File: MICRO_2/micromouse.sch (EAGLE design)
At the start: 26 parts

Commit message: Add files via upload
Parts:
- removed C1: (no value), capacitor-wima:C2,5-3
- removed R1, R2, R3, R4, R5: 10k, rcl:R-US_0204/5
- removed R10, R6, R7, R8, R9: 330, rcl:R-US_0204/5
- removed U$15: VOLTAGE_REGULATOR, VOLTAGE_REGULATOR:VOLTAGE_REGULATOR
- U$1: value TEENSY3.2 -> MOTOR_ENCODER; device teensy_3.2:TEENSY3.2 -> MOTOR_ENCODER:MOTOR_ENCODER
- U$10, U$11, U$12: value IR_EMITTER -> IR_RECIEVER; device IR_EMITTER:IR_EMITTER -> IR_RECIEVER:IR_RECIEVER
- U$13, U$14: value MOTOR_ENCODER -> IR_RECIEVER; device MOTOR_ENCODER:MOTOR_ENCODER -> IR_RECIEVER:IR_RECIEVER
- U$2: value MOTOR_DRIVER -> MOTOR_ENCODER; device motor_driver:MOTOR_DRIVER -> MOTOR_ENCODER:MOTOR_ENCODER
- U$3: value IR_RECIEVER -> TEENSY_3.1-3.2_DIL; device IR_RECIEVER:IR_RECIEVER -> Teensy_3_and_LC_Series_Boards_v1.4:TEENSY_3.1-3.2_DIL
- U$4: value IR_RECIEVER -> MOTOR_DRIVER; device IR_RECIEVER:IR_RECIEVER -> motor_driver:MOTOR_DRIVER
- U$5, U$6, U$7: value IR_RECIEVER -> IR_EMITTER; device IR_RECIEVER:IR_RECIEVER -> IR_EMITTER:IR_EMITTER
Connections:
- removed net GND: C1.2, R1.1, R2.2, R3.1, R4.1, R5.2, U$1.GND, U$10.EMI_CATHODE, U$11.EMI_CATHODE, U$12.EMI_CATHODE, U$13.GND, U$14.GND, U$15.GND, U$2.L_GND_1, U$2.L_GND_2, U$2.R_GND_1, U$2.R_GND_2, U$8.EMI_CATHODE, U$9.EMI_CATHODE
- removed net N$1: U$1.2, U$2.M1_ENABLE
- removed net N$10: R6.1, U$1.0
- removed net N$11: R7.1, U$9.EMI_ANODE
- removed net N$12: R7.2, U$1.7
- removed net N$13: R8.1, U$10.EMI_ANODE
- removed net N$14: R8.2, U$1.8
- removed net N$15: R9.1, U$11.EMI_ANODE
- removed net N$16: R9.2, U$1.11
- removed net N$17: R10.1, U$12.EMI_ANODE
- removed net N$18: R10.2, U$1.12
- removed net N$19: R1.2, U$1.15, U$4.REC_CATHODE
- removed net N$2: U$1.3, U$2.M1_FWD_PWN
- removed net N$20: R2.1, U$1.16, U$5.REC_CATHODE
- removed net N$21: R4.2, U$1.17, U$6.REC_CATHODE
- removed net N$22: R5.1, U$1.18, U$7.REC_CATHODE
- removed net N$24: R3.2, U$1.14, U$3.REC_CATHODE
- removed net N$25: U$13.M1, U$2.L_M1_1
- removed net N$26: U$1.20, U$14.OUTB
- removed net N$27: U$1.13, U$13.OUTA
- removed net N$28: U$1.21, U$14.OUTA
- removed net N$29: U$1.19, U$13.OUTB
- removed net N$3: U$13.M2, U$2.L_M1_2
- removed net N$30: C1.1, U$1.26, U$13.VCC, U$14.VCC, U$15.VOUT, U$2.L_5V, U$2.R_5V
- removed net N$32: U$14.M1, U$2.R_M2_1
- removed net N$36: U$1.24, U$3.REC_ANODE, U$4.REC_ANODE, U$5.REC_ANODE, U$6.REC_ANODE, U$7.REC_ANODE
- removed net N$4: U$1.1, U$2.M2_ENABLE
- removed net N$5: U$1.5, U$2.M2_REV_PWM
- removed net N$6: U$14.M2, U$2.R_M2_2
- removed net N$7: U$1.6, U$2.M2_FWD_PWM
- removed net N$8: U$1.4, U$2.M1_REV_PWN
- removed net N$9: R6.2, U$8.EMI_ANODE

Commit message: Add files via upload
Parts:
- removed U$13, U$14: IR_RECIEVER, IR_RECIEVER:IR_RECIEVER
- added R1, R3, R5: 330, rcl:R-US_0207/10
- added R2, R4: 10K, rcl:R-US_0207/10
- added R6: 10k, rcl:R-US_0207/10
- U$10: value IR_RECIEVER -> VOLTAGE_REGULATOR; device IR_RECIEVER:IR_RECIEVER -> VOLTAGE_REGULATOR:VOLTAGE_REGULATOR
- U$11: value IR_RECIEVER -> BATTERY_INPUT; device IR_RECIEVER:IR_RECIEVER -> Battery_input:BATTERY_INPUT
- U$5, U$8: value IR_EMITTER -> IR_RECIEVER; device IR_EMITTER:IR_EMITTER -> IR_RECIEVER:IR_RECIEVER
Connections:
- new net N$1: U$10.VIN, U$11.VIN
- new net N$10: U$3.13/SCK/LED, U$4.M2_ENABLE
- new net N$11: U$1.M1, U$4.L_M1_1
- new net N$12: U$1.M2, U$4.L_M1_2
- new net N$13: U$2.M1, U$4.R_M2_1
- new net N$14: U$2.M2, U$4.R_M2_2
- new net N$15: U$1.OUTA, U$3.10/TX2/PWM
- new net N$16: U$1.OUTB, U$3.11/MOSI
- new net N$17: U$2.OUTB, U$3.8/TX3
- new net N$18: U$2.OUTA, U$3.9/RX2/PWM
- new net N$2: U$1.GND, U$10.GND, U$11.GND, U$2.GND, U$3.GND, U$4.L_GND_1, U$4.L_GND_2, U$4.R_GND_1, U$4.R_GND_2
- new net N$3: U$1.VCC, U$10.VOUT, U$2.VCC, U$3.VIN, U$4.L_5V, U$4.R_5V
- new net N$4: U$3.12/MISO, U$4.M1_ENABLE
- new net N$5: U$3.3.3V
- new net N$6: U$3.20/A6/PWM, U$4.M1_FWD_PWN
- new net N$7: U$3.21/A7/PWM, U$4.M1_REV_PWN
- new net N$8: U$3.22/A8/T/PWM, U$4.M2_REV_PWM
- new net N$9: U$3.23/A9/T/PWM, U$4.M2_FWD_PWM
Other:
- moved on the sheet: U$3

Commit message: Add files via upload
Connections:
- new net N$19: R1.2, U$3.0/RX1/T
- new net N$20: R1.1, U$9.EMI_ANODE
- new net N$21: R6.1, U$3.14/A1, U$8.REC_CATHODE
- new net N$22: R3.2, U$3.1/TX1/T
- new net N$23: R3.1, U$6.EMI_ANODE
- new net N$24: R4.1, U$12.REC_CATHODE, U$3.15/A1/T
- new net N$25: R5.2, U$3.2
- new net N$26: R5.1, U$7.EMI_ANODE
- new net N$28: R2.1, U$3.16/A2/T, U$5.REC_CATHODE
- net N$2: now also R2.2, R4.2, R6.2, U$6.EMI_CATHODE, U$7.EMI_CATHODE, U$9.EMI_CATHODE
- net N$5: now also U$12.REC_ANODE, U$5.REC_ANODE, U$8.REC_ANODE
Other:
- moved on the sheet: R1, R2, R3, R4, R5, R6

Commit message: Add files via upload
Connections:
- removed net N$2: R2.2, R4.2, R6.2, U$1.GND, U$10.GND, U$11.GND, U$2.GND, U$3.GND, U$4.L_GND_1, U$4.L_GND_2, U$4.R_GND_1, U$4.R_GND_2, U$6.EMI_CATHODE, U$7.EMI_CATHODE, U$9.EMI_CATHODE
- new net GND: R2.2, R4.2, R6.2, U$1.GND, U$10.GND, U$11.BAT_GND, U$2.GND, U$3.GND, U$4.L_GND_1, U$4.L_GND_2, U$4.R_GND_1, U$4.R_GND_2, U$6.EMI_CATHODE, U$7.EMI_CATHODE, U$9.EMI_CATHODE
- net N$1: now also U$11.BAT_7.4V; no longer U$11.VIN
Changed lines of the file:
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@@
 <net name="N$1" class="0">
 <segment>
-<pinref part="U$11" gate="G$1" pin="VIN"/>
 <wire x1="88.9" y1="-10.16" x2="88.9" y2="-22.86" width="0.1524" layer="91"/>
 <pinref part="U$10" gate="G$1" pin="VIN"/>
 <wire x1="88.9" y1="-22.86" x2="55.88" y2="-22.86" width="0.1524" layer="91"/>
 <wire x1="55.88" y1="-22.86" x2="55.88" y2="-10.16" width="0.1524" layer="91"/>
-</segment>
-</net>
-<net name="N$2" class="0">
-<segment>
-<pinref part="U$11" gate="G$1" pin="GND"/>
+<pinref part="U$11" gate="G$1" pin="BAT_7.4V"/>
+</segment>
+</net>
+<net name="GND" class="0">
+<segment>
 <wire x1="93.98" y1="-10.16" x2="93.98" y2="-15.24" width="0.1524" layer="91"/>
 <wire x1="93.98" y1="-15.24" x2="58.42" y2="-15.24" width="0.1524" layer="91"/>
@@
 <wire x1="45.72" y1="55.88" x2="45.72" y2="33.02" width="0.1524" layer="91"/>
 <junction x="45.72" y="33.02"/>
+<pinref part="U$11" gate="G$1" pin="BAT_GND"/>
 </segment>
 </net>
@@
 </sheet>
 </sheets>
+<errors>
+</errors>
 </schematic>
 </drawing>

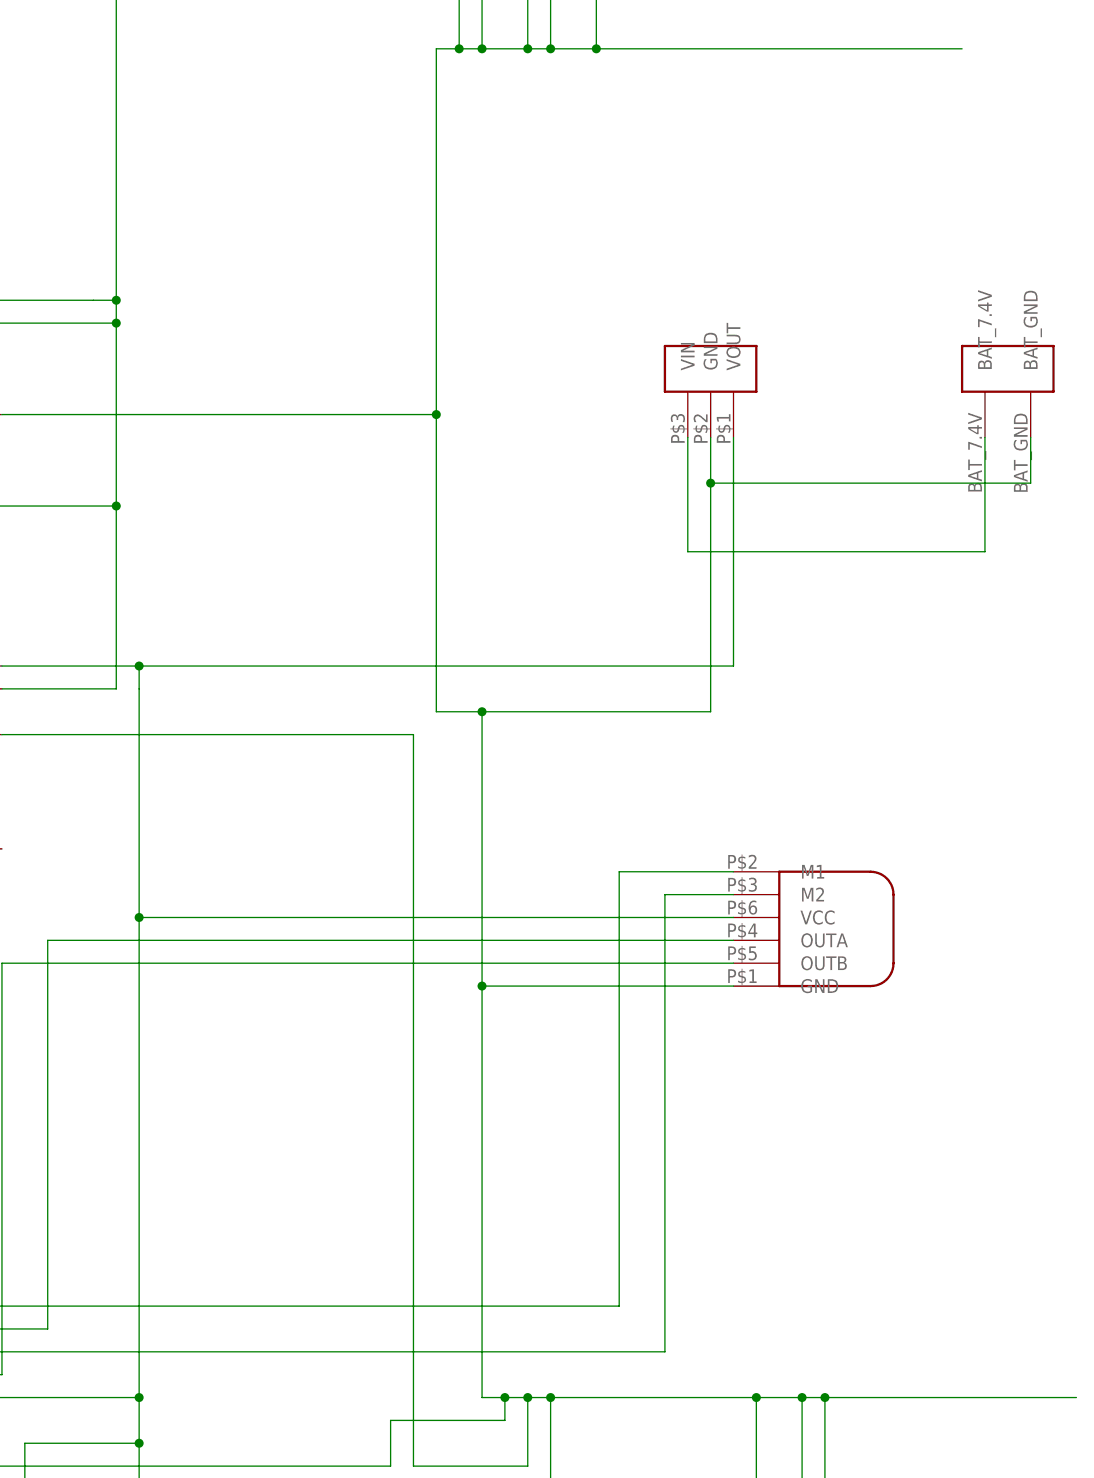
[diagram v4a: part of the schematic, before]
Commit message: added imu component
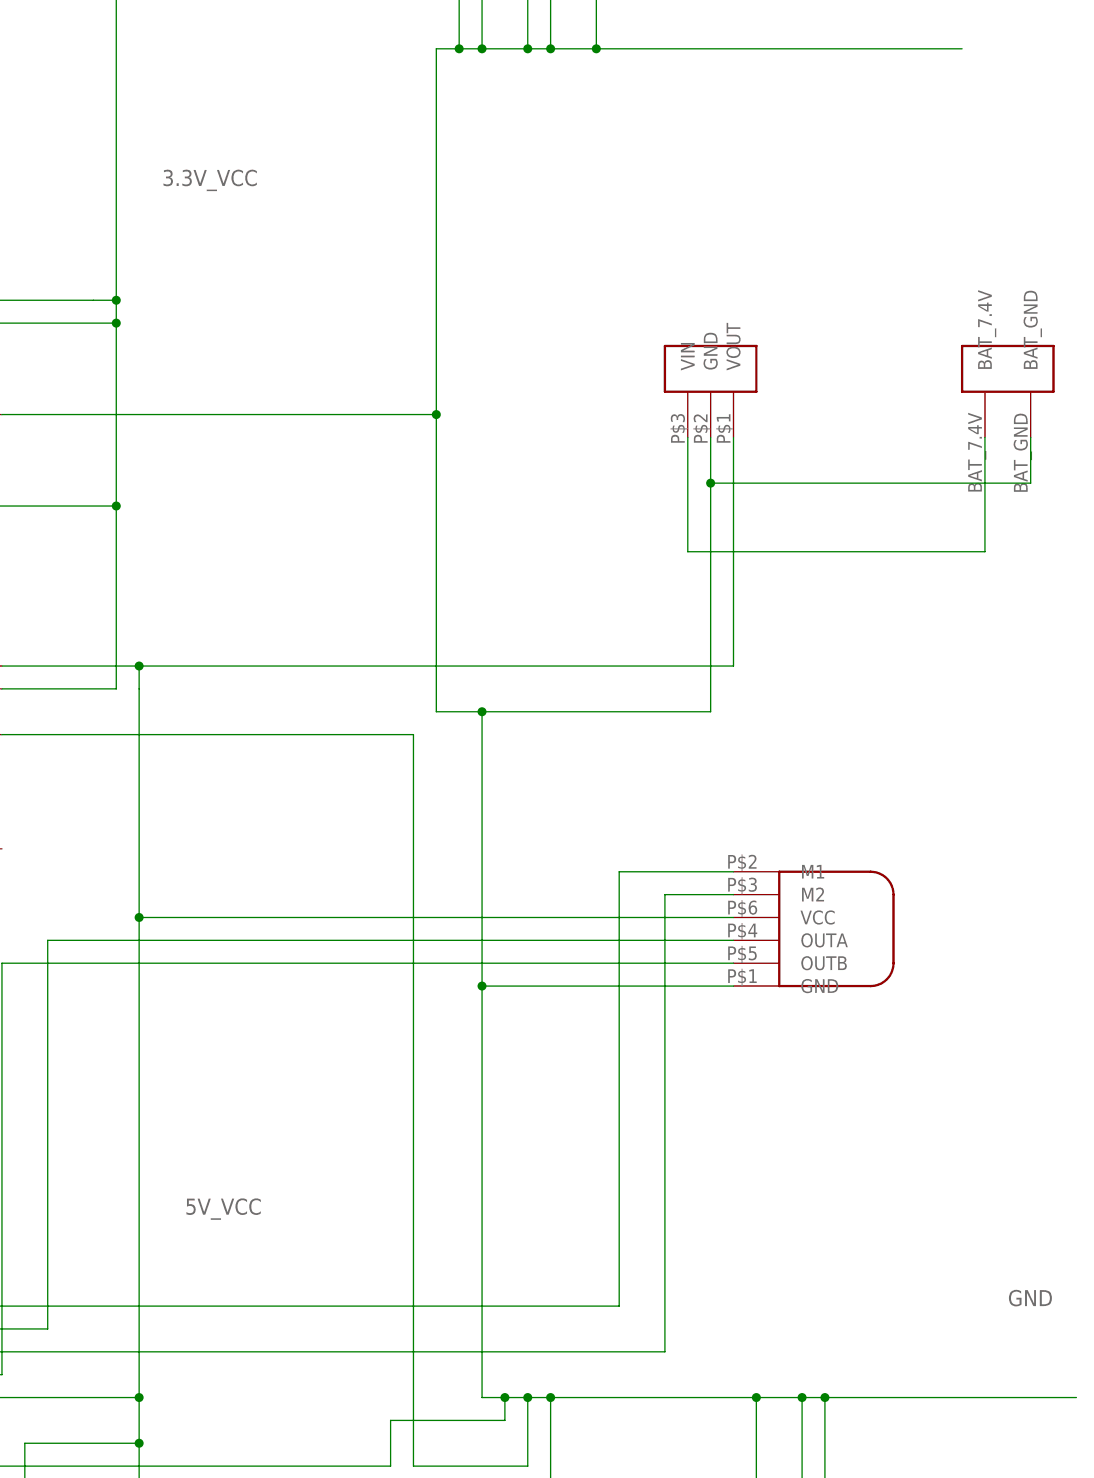
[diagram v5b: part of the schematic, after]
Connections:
- net N$3 renamed 5V_VCC
- net N$5 renamed 3.3V_VCC
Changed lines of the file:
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@@
 <junction x="45.72" y="33.02"/>
 <pinref part="U$11" gate="G$1" pin="BAT_GND"/>
+<label x="91.44" y="-106.68" size="1.778" layer="95"/>
 </segment>
 </net>
-<net name="N$3" class="0">
+<net name="5V_VCC" class="0">
 <segment>
 <pinref part="U$10" gate="G$1" pin="VOUT"/>
@@
 <wire x1="-5.08" y1="-35.56" x2="-5.08" y2="-38.1" width="0.1524" layer="91"/>
 <junction x="-5.08" y="-35.56"/>
+<label x="0" y="-96.52" size="1.778" layer="95"/>
 </segment>
 </net>
-<net name="N$5" class="0">
+<net name="3.3V_VCC" class="0">
 <segment>
 <pinref part="U$3" gate="G$1" pin="3.3V"/>
@@
 <wire x1="-10.16" y1="5.08" x2="-7.62" y2="5.08" width="0.1524" layer="91"/>
 <junction x="-7.62" y="5.08"/>
+<label x="-2.54" y="17.78" size="1.778" layer="95"/>
 </segment>
 </net>

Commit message: Add files via upload
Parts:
- added U$13: IMU, IMU:IMU
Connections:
- net N$10 renamed M2_ENABLE
- net N$11 renamed M1_L
- net N$12 renamed M2_L
- net N$13 renamed M1_R
- net N$14 renamed M2_R
- net N$15 renamed OUTA_L
- net N$16 renamed OUTB_L
- net N$17 renamed OUTB_R
- net N$18 renamed OUTA_R
- net N$6 renamed M1_FWD_PWM
- net N$7 renamed M1_REV_PWM
- net N$8 renamed M2_REV_PWM
- net N$9 renamed M2_FWD_PWM
- new net N$2: U$13.SCL, U$3.19/A5/T/SCL0
- new net N$3: U$13.SDA, U$3.18/A4/T/SDA0
- net 5V_VCC: now also U$13.5V
- net GND: now also U$13.GND
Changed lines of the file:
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@@
 <part name="U$10" library="VOLTAGE_REGULATOR" deviceset="VOLTAGE_REGULATOR" device=""/>
 <part name="U$11" library="Battery_input" deviceset="BATTERY_INPUT" device=""/>
+<part name="U$13" library="IMU" deviceset="IMU" device=""/>
 </parts>
 <sheets>
@@
 <instance part="U$10" gate="G$1" x="43.18" y="2.54" rot="R180"/>
 <instance part="U$11" gate="G$1" x="101.6" y="0"/>
+<instance part="U$13" gate="G$1" x="-165.1" y="-45.72" rot="R180"/>
 </instances>
 <busses>
@@
 <wire x1="63.5" y1="-116.84" x2="68.58" y2="-116.84" width="0.1524" layer="91"/>
 <wire x1="68.58" y1="-116.84" x2="71.12" y2="-116.84" width="0.1524" layer="91"/>
-<wire x1="71.12" y1="-116.84" x2="99.06" y2="-116.84" width="0.1524" layer="91"/>
+<wire x1="71.12" y1="-116.84" x2="73.66" y2="-116.84" width="0.1524" layer="91"/>
+<wire x1="73.66" y1="-116.84" x2="99.06" y2="-116.84" width="0.1524" layer="91"/>
 <wire x1="-20.32" y1="-43.18" x2="25.4" y2="-43.18" width="0.1524" layer="91"/>
 <wire x1="25.4" y1="-43.18" x2="25.4" y2="-124.46" width="0.1524" layer="91"/>
@@
 <pinref part="U$11" gate="G$1" pin="BAT_GND"/>
 <label x="91.44" y="-106.68" size="1.778" layer="95"/>
+<pinref part="U$13" gate="G$1" pin="GND"/>
+<wire x1="-144.78" y1="-50.8" x2="-139.7" y2="-50.8" width="0.1524" layer="91"/>
+<wire x1="-139.7" y1="-50.8" x2="-139.7" y2="-106.68" width="0.1524" layer="91"/>
+<wire x1="-139.7" y1="-106.68" x2="-205.74" y2="-106.68" width="0.1524" layer="91"/>
+<wire x1="-205.74" y1="-106.68" x2="-205.74" y2="-177.8" width="0.1524" layer="91"/>
+<wire x1="-205.74" y1="-177.8" x2="73.66" y2="-177.8" width="0.1524" layer="91"/>
+<wire x1="73.66" y1="-177.8" x2="73.66" y2="-116.84" width="0.1524" layer="91"/>
+<junction x="73.66" y="-116.84"/>
 </segment>
 </net>
@@
 <wire x1="60.96" y1="-35.56" x2="-5.08" y2="-35.56" width="0.1524" layer="91"/>
 <wire x1="-20.32" y1="-35.56" x2="-5.08" y2="-35.56" width="0.1524" layer="91"/>
-<wire x1="-5.08" y1="-38.1" x2="-5.08" y2="-63.5" width="0.1524" layer="91"/>
+<wire x1="-5.08" y1="-35.56" x2="-5.08" y2="-63.5" width="0.1524" layer="91"/>
 <wire x1="-5.08" y1="-63.5" x2="-5.08" y2="-116.84" width="0.1524" layer="91"/>
 <wire x1="-5.08" y1="-116.84" x2="-5.08" y2="-121.92" width="0.1524" layer="91"/>
@@
 <wire x1="-5.08" y1="-132.08" x2="2.54" y2="-132.08" width="0.1524" layer="91"/>
 <pinref part="U$4" gate="G$1" pin="R_5V"/>
-<wire x1="2.54" y1="-132.08" x2="53.34" y2="-132.08" width="0.1524" layer="91"/>
+<wire x1="2.54" y1="-132.08" x2="7.62" y2="-132.08" width="0.1524" layer="91"/>
+<wire x1="7.62" y1="-132.08" x2="53.34" y2="-132.08" width="0.1524" layer="91"/>
 <wire x1="-104.14" y1="-116.84" x2="-5.08" y2="-116.84" width="0.1524" layer="91"/>
 <junction x="-5.08" y="-116.84"/>
@@
 <wire x1="60.96" y1="-63.5" x2="-5.08" y2="-63.5" width="0.1524" layer="91"/>
 <junction x="-5.08" y="-63.5"/>
-<wire x1="-5.08" y1="-35.56" x2="-5.08" y2="-38.1" width="0.1524" layer="91"/>
 <junction x="-5.08" y="-35.56"/>
 <label x="0" y="-96.52" size="1.778" layer="95"/>
+<pinref part="U$13" gate="G$1" pin="5V"/>
+<wire x1="-144.78" y1="-55.88" x2="-142.24" y2="-55.88" width="0.1524" layer="91"/>
+<wire x1="-142.24" y1="-55.88" x2="-142.24" y2="-104.14" width="0.1524" layer="91"/>
+<wire x1="-142.24" y1="-104.14" x2="-208.28" y2="-104.14" width="0.1524" layer="91"/>
+<wire x1="-208.28" y1="-104.14" x2="-208.28" y2="-182.88" width="0.1524" layer="91"/>
+<wire x1="-208.28" y1="-182.88" x2="7.62" y2="-182.88" width="0.1524" layer="91"/>
+<wire x1="7.62" y1="-182.88" x2="7.62" y2="-132.08" width="0.1524" layer="91"/>
+<junction x="7.62" y="-132.08"/>
 </segment>
 </net>
@@
 </segment>
 </net>
-<net name="N$6" class="0">
+<net name="M1_FWD_PWM" class="0">
 <segment>
 <pinref part="U$4" gate="G$1" pin="M1_FWD_PWN"/>
@@
 </segment>
 </net>
-<net name="N$7" class="0">
+<net name="M1_REV_PWM" class="0">
 <segment>
 <pinref part="U$4" gate="G$1" pin="M1_REV_PWN"/>
@@
 </segment>
 </net>
-<net name="N$8" class="0">
+<net name="M2_REV_PWM" class="0">
 <segment>
 <pinref part="U$4" gate="G$1" pin="M2_REV_PWM"/>
@@
 </segment>
 </net>
-<net name="N$9" class="0">
+<net name="M2_FWD_PWM" class="0">
 <segment>
 <pinref part="U$4" gate="G$1" pin="M2_FWD_PWM"/>
@@
 </segment>
 </net>
-<net name="N$11" class="0">
+<net name="M1_L" class="0">
 <segment>
 <pinref part="U$4" gate="G$1" pin="L_M1_1"/>
@@
 </segment>
 </net>
-<net name="N$12" class="0">
+<net name="M2_L" class="0">
 <segment>
 <pinref part="U$4" gate="G$1" pin="L_M1_2"/>
@@
 </segment>
 </net>
-<net name="N$13" class="0">
+<net name="M1_R" class="0">
 <segment>
 <pinref part="U$4" gate="G$1" pin="R_M2_1"/>
@@
 </segment>
 </net>
-<net name="N$14" class="0">
+<net name="M2_R" class="0">
 <segment>
 <pinref part="U$2" gate="G$1" pin="M2"/>
@@
 </segment>
 </net>
-<net name="N$10" class="0">
+<net name="M2_ENABLE" class="0">
 <segment>
 <pinref part="U$4" gate="G$1" pin="M2_ENABLE"/>
@@
 </segment>
 </net>
-<net name="N$15" class="0">
+<net name="OUTA_L" class="0">
 <segment>
 <pinref part="U$1" gate="G$1" pin="OUTA"/>
@@
 </segment>
 </net>
-<net name="N$16" class="0">
+<net name="OUTB_L" class="0">
 <segment>
 <pinref part="U$1" gate="G$1" pin="OUTB"/>
@@
 </segment>
 </net>
-<net name="N$17" class="0">
+<net name="OUTB_R" class="0">
 <segment>
 <pinref part="U$2" gate="G$1" pin="OUTB"/>
@@
 </segment>
 </net>
-<net name="N$18" class="0">
+<net name="OUTA_R" class="0">
 <segment>
 <pinref part="U$2" gate="G$1" pin="OUTA"/>
@@
 </segment>
 </net>
+<net name="N$2" class="0">
+<segment>
+<pinref part="U$13" gate="G$1" pin="SCL"/>
+<wire x1="-144.78" y1="-40.64" x2="-134.62" y2="-40.64" width="0.1524" layer="91"/>
+<wire x1="-134.62" y1="-40.64" x2="-134.62" y2="-83.82" width="0.1524" layer="91"/>
+<pinref part="U$3" gate="G$1" pin="19/A5/T/SCL0"/>
+<wire x1="-134.62" y1="-83.82" x2="-66.04" y2="-83.82" width="0.1524" layer="91"/>
+</segment>
+</net>
+<net name="N$3" class="0">
+<segment>
+<pinref part="U$13" gate="G$1" pin="SDA"/>
+<wire x1="-144.78" y1="-45.72" x2="-137.16" y2="-45.72" width="0.1524" layer="91"/>
+<pinref part="U$3" gate="G$1" pin="18/A4/T/SDA0"/>
+<wire x1="-137.16" y1="-45.72" x2="-137.16" y2="-81.28" width="0.1524" layer="91"/>
+<wire x1="-137.16" y1="-81.28" x2="-66.04" y2="-81.28" width="0.1524" layer="91"/>
+</segment>
+</net>

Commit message: added 2 extra ir pairs
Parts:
- added R10, R8: 10K, rcl:R-US_0207/10
- added R7, R9: 330, rcl:R-US_0207/10
- added U$14, U$16: IR_EMITTER, IR_EMITTER:IR_EMITTER
- added U$15, U$17: IR_RECIEVER, IR_RECIEVER:IR_RECIEVER
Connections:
- removed net M2_REV_PWM: U$3.22/A8/T/PWM, U$4.M2_REV_PWM
- new net N$10: R9.1, U$16.EMI_ANODE
- new net N$12: R10.1, U$17.REC_CATHODE, U$3.23/A9/T/PWM
- new net N$5: U$3.5/PWM, U$4.M2_REV_PWM
- new net N$6: R7.2, U$3.3/CAN-TX/PWM
- new net N$7: R7.1, U$14.EMI_ANODE
- new net N$8: R8.1, U$15.REC_CATHODE, U$3.22/A8/T/PWM
- new net N$9: R9.2, U$3.4/CAN-RX/PWM
- net 3.3V_VCC: now also U$15.REC_ANODE, U$17.REC_ANODE
- net GND: now also R10.2, R8.2, U$14.EMI_CATHODE, U$16.EMI_CATHODE
- net M2_FWD_PWM: now also U$3.6/PWM; no longer U$3.23/A9/T/PWM
